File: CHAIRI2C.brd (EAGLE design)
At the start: 34 x 34 mm, 20 parts, among them IC1 DS3502, IC2 DS3502, X1 OUTPUT

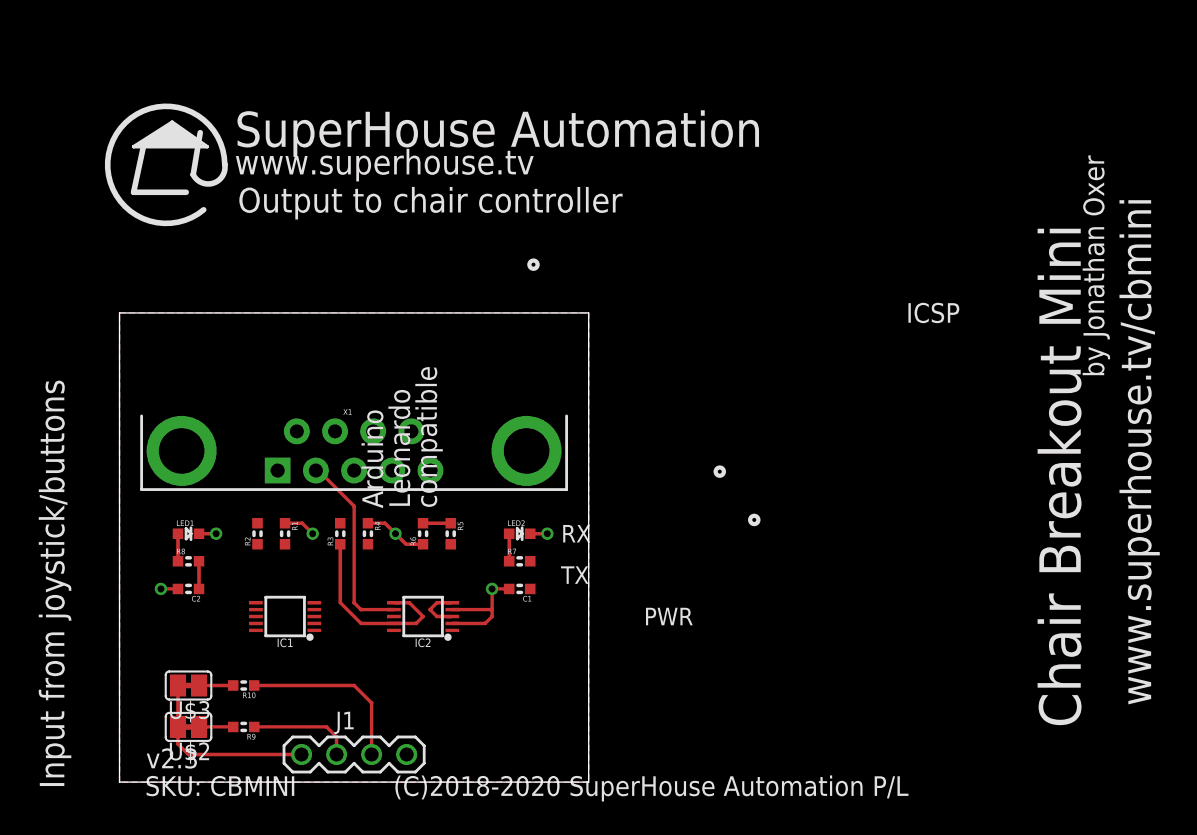
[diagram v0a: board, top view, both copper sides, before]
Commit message: Changed VREF on digital pots for v1.0 release
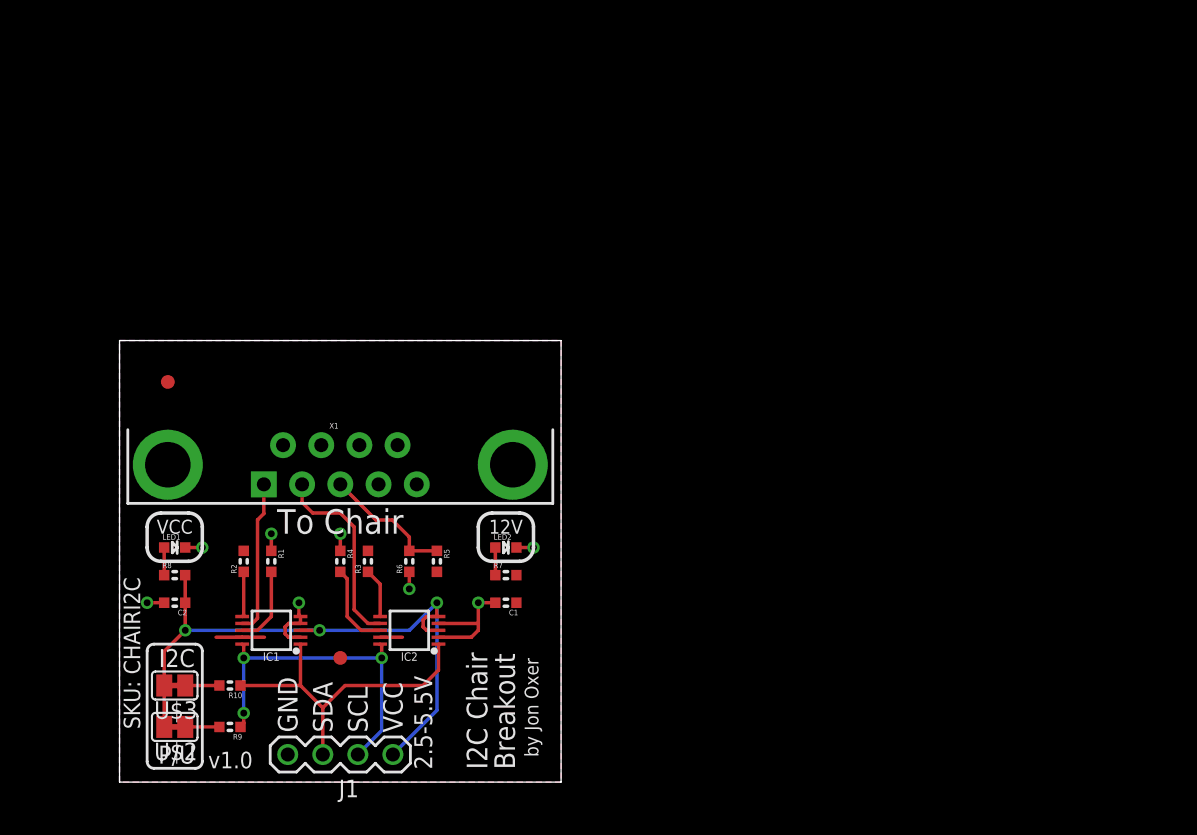
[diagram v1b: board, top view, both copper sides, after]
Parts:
- added U$8, U$9: FIDUCIAL1X2.5, SuperHouse-Symbols:FIDUCIAL-1X2.5
- moved R3 2.83 mm to (18.0, 18.0)
- moved R4 2.83 mm to (16.0, 18.0)
- moved R1 2.24 mm to (11.0, 18.0)
- moved R2 2.24 mm to (9.00, 18.0)
- moved R5 2.24 mm to (23.0, 18.0)
- moved R6 2.24 mm to (21.0, 18.0)
- moved C1 1.41 mm to (28.0, 15.0)
- moved C2 1.41 mm to (4.00, 15.0)
- moved IC1 1.41 mm to (11.0, 13.0)
- moved IC2 1.41 mm to (21.0, 13.0)
- moved LED1 1.41 mm to (4.00, 19.0)
- moved LED2 1.41 mm to (28.0, 19.0)
- moved R7 1.41 mm to (28.0, 17.0)
- moved R8 1.41 mm to (4.00, 17.0)
- moved X1 1.41 mm to (16.0, 25.0)
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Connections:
- net 12V: now also IC1.9, IC2.9
- net N$2: no longer IC1.9
- net N$3: no longer IC2.9
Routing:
- net VCC: track 19.1 -> 48.3 mm, vias 0 -> 3
- net SCL: track 7.54 -> 24.9 mm, vias 0 -> 3
- net SDA: track 12.8 -> 24.4 mm
- net SPEED_OUT: track 0.00 -> 11.2 mm
- net N$3: track 13.6 -> 3.61 mm
- net VREF: track 2.00 -> 9.58 mm
- net N$15: track 0.00 -> 6.25 mm
- net N$4: track 0.00 -> 5.77 mm
- net 12V: track 0.00 -> 5.11 mm
- net N$2: track 0.00 -> 3.28 mm
- net GND: track 19.9 -> 21.1 mm, vias 6 -> 8
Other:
- board size 34 x 34 mm -> 32 x 32 mm
- board text added: "(C)2020 SuperHouse Automation"
- board text added: "12V"
- board text added: "2.5-5.5V"
- board text added: "Breakout"
- board text added: "GND"
- board text added: "I2C"
- board text added: "I2C Chair"
- board text added: "P/U"
- board text added: "SCL"
- board text added: "SDA"
- board text added: "SKU: CHAIRI2C"
- board text added: "Super House"
- board text added: "To Chair"
- board text added: "VCC"
- board text added: "by Jon Oxer"
- board text added: "v1.0"
- board text added: "www.superhouse.tv/chairi2c"
- board text removed: "(C)2018-2020 SuperHouse Automation P/L"
- board text removed: "Arduino Leonardo compatible"
- board text removed: "Chair Breakout Mini"
- board text removed: "ICSP"
- board text removed: "Input from joystick/buttons"
- board text removed: "Output to chair controller"
- board text removed: "PWR"
- board text removed: "RX"
- board text removed: "SKU: CBMINI"
- board text removed: "SuperHouse Automation"
- board text removed: "TX"
- board text removed: "by Jonathan Oxer"
- board text removed: "v2.3"
- board text removed: "www.superhouse.tv"
- board text removed: "www.superhouse.tv/cbmini"

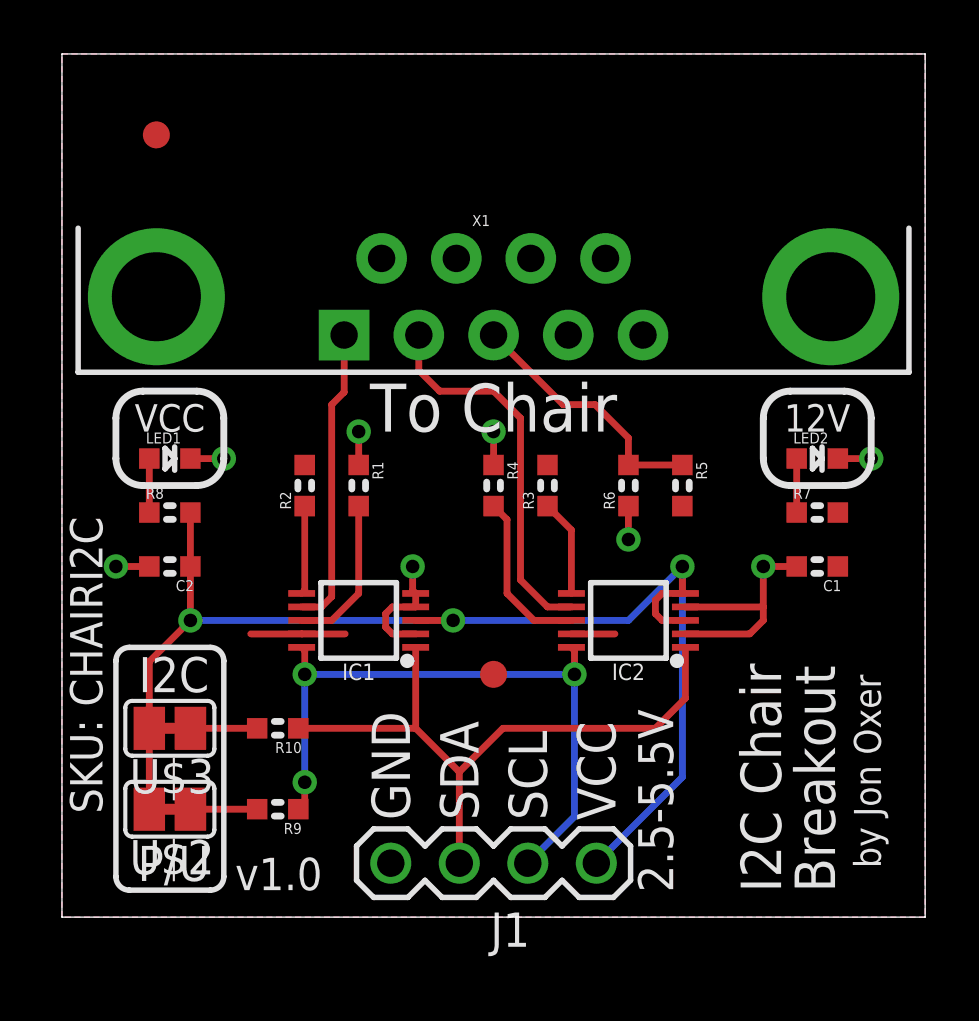
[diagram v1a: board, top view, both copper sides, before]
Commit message: Changed reference bias and exposed extra connections
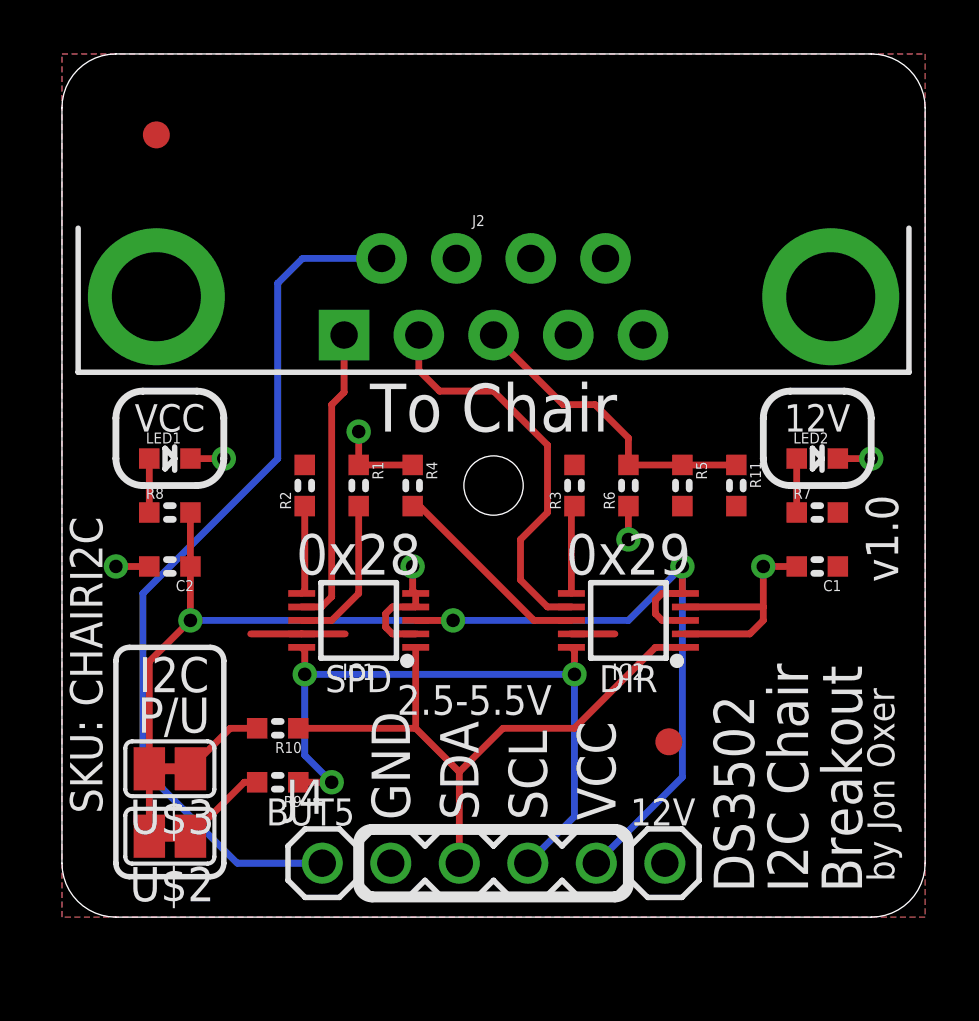
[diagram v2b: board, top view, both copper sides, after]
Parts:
- removed J1: (no value), SuperHouse-Connectors:1X04
- added J4: M06-PLAIN, SuperHouse-Connectors:1X06
- added R11: 22K, SuperHouse-DiscreteSemi:R0603
- R5, R6: value 22K -> 1K
- moved U$9 6.96 mm to (22.5, 8.50)
- moved R4 3.00 mm to (13.0, 18.0)
- moved U$3 1.50 mm to (4.00, 7.50)
- moved R3 1.00 mm to (19.0, 18.0)
- moved R9 1.00 mm to (8.00, 7.00)
- moved U$2 1.00 mm to (4.00, 5.00)
- renumbered X1 to J2
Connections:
- removed net DETECT: J2.5
- removed net PIN4: J2.4
- removed net PIN6: J2.6
- new net BUT5: J2.6, J4.1
- net 12V: now also J4.6, R11.2
- net GND: now also J2.5, J4.2; no longer J1.4
- net SCL: now also J4.4; no longer J1.2
- net SDA: now also J4.3; no longer J1.3
- net VCC: now also J4.5; no longer J1.1
- net VREF: now also R11.1
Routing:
- net BUT5: track 0.00 -> 32.4 mm
- net VREF: track 9.58 -> 11.6 mm
- net N$15: track 6.25 -> 7.64 mm
- net SDA: track 24.4 -> 23.3 mm
- net VCC: track 48.3 -> 49.3 mm
- net N$1: track 2.48 -> 3.30 mm
- net DIRECTION_OUT: track 14.1 -> 14.9 mm
- net GND: track 21.1 -> 21.9 mm, vias 8 -> 7
- net N$8: track 2.48 -> 3.11 mm
- net SCL: track 24.9 -> 25.5 mm
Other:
- outline, holes or cut-outs redrawn
- board text added: "0x28"
- board text added: "0x29"
- board text added: "BUT5"
- board text added: "DIR"
- board text added: "DS3502"
- board text added: "SPD"
